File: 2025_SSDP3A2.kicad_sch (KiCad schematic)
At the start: 58 parts, among them J1 SolderPad, J2 SolderPad, J3 SolderPad, J4 SolderPad, Q1 CSD19534Q5A, Q2 BSC0805LS, U1 LM5146RGYR

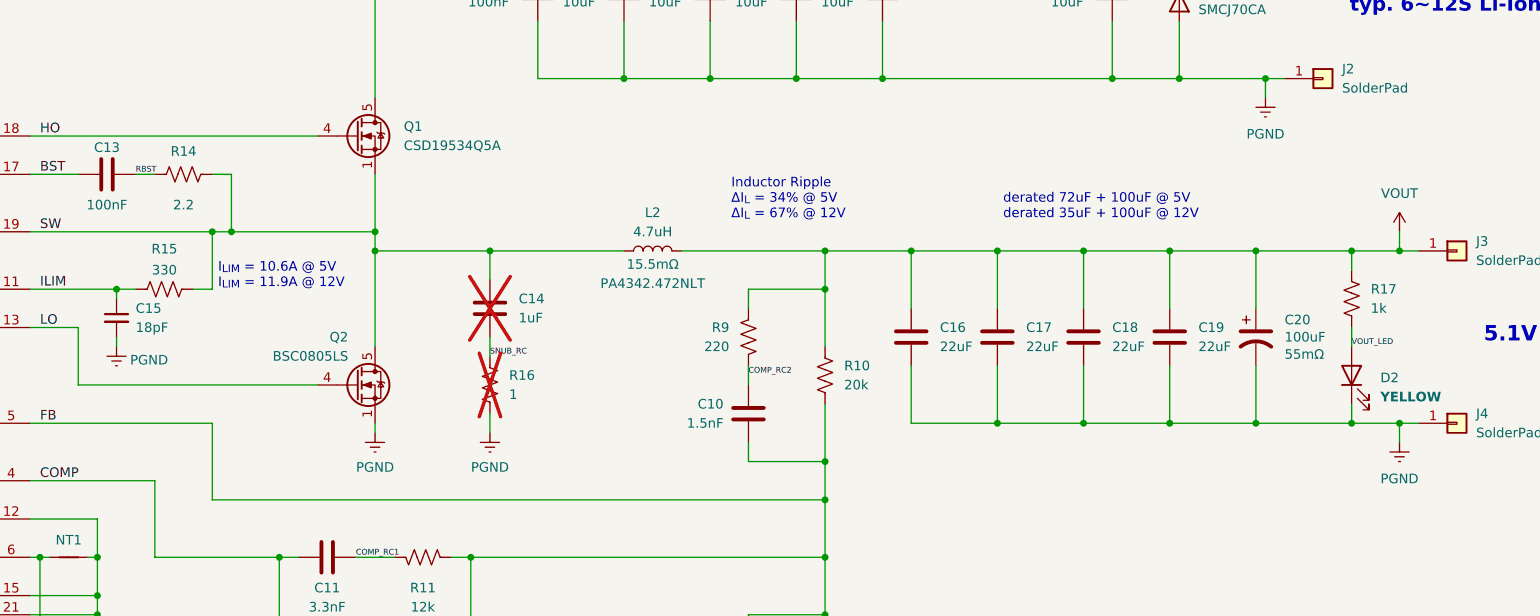
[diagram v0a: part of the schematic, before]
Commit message: Using PQFN FETs instead of SuperSO-8
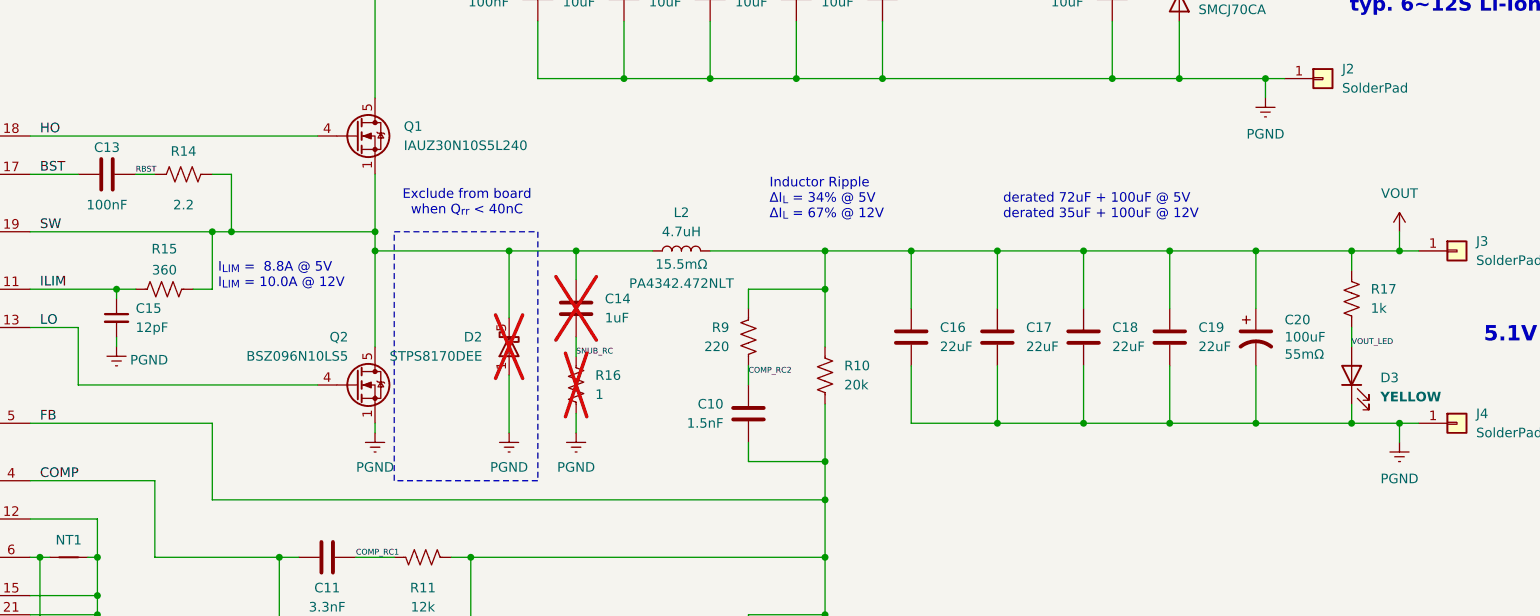
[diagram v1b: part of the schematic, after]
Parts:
- added D2: STPS8170DEE, TSDSON-8:PG-TSDSON-8-26, symbol Device:D_Schottky_AAK
- C15: value 18pF -> 12pF; LCSC PN C913624 -> C576801; MANUFACTURER Murata Electronics -> YAGEO
- Q1: value CSD19534Q5A -> IAUZ30N10S5L240; footprint Package_TO_SOT_SMD:TDSON-8-1 -> TSDSON-8:PG-TSDSON-8-26_TV; ESR 13.8mΩ -> 26.0mΩ; LCSC PN C114200 -> C535732; MANUFACTURER Texas Instruments -> Infineon Technologies
- Q2: value BSC0805LS -> BSZ096N10LS5; footprint Package_TO_SOT_SMD:TDSON-8-1 -> TSDSON-8:PG-TSDSON-8-26; ESR 7.1mΩ -> 9.6mΩ; LCSC PN C534374 -> C534695
- R15: value 330 -> 360; LCSC PN C23138 -> C25194; Part Type Basic -> Preferred Extended
- renumbered D2 to D3
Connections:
- net PGND: now also D2.1 (A), D2.2 (A), D2.3 (A)
- net SW: now also Q2.6 (D), Q2.7 (D), Q2.8 (D), D2.5 (K), D2.6, D2.7, D2.8
- net VIN: now also Q1.6 (D), Q1.7 (D), Q1.8 (D)
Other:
- note added: "Exclude from board when Q_{rr} < 40nC"
- note added: "I_{LIM} = 8.8A @ 5V I_{LIM} = 10.0A @ 12V"
- note removed: "I_{LIM} = 10.6A @ 5V I_{LIM} = 11.9A @ 12V"
- moved on the sheet: L2

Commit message: Finished routing
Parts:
- R7: value 27k -> 24k; LCSC PN C22967 -> C23352
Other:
- note added: "f_{SW} = 420kHz"
- note removed: "f_{SW} = 370kHz"
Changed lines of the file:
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@@
 		)
 	)
-	(text "f_{SW} = 370kHz"
+	(text "f_{SW} = 420kHz"
 		(exclude_from_sim no)
 		(at 69.85 135.636 0)
@@
 			)
 		)
-		(property "Value" "27k"
+		(property "Value" "24k"
 			(at 72.39 175.26 0)
 			(effects
@@
 			)
 		)
-		(property "Description" "0603WAF2702T5E"
+		(property "Description" "0603WAF2402T5E"
 			(at 69.85 173.99 0)
 			(effects
@@
 			)
 		)
-		(property "LCSC PN" "C22967"
+		(property "LCSC PN" "C23352"
 			(at 69.85 173.99 0)
 			(effects

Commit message: Tweaked routing, changed some fab parameters
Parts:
- Q1, Q2, U1: FT Rotation Offset -90 -> 0
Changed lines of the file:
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@@
 			)
 		)
-		(property "FT Rotation Offset" "-90"
+		(property "FT Rotation Offset" "0"
 			(at 114.3 116.84 0)
 			(effects
@@
 			)
 		)
-		(property "FT Rotation Offset" "-90"
+		(property "FT Rotation Offset" "0"
 			(at 203.2 116.84 0)
 			(effects
@@
 			)
 		)
-		(property "FT Rotation Offset" "-90"
+		(property "FT Rotation Offset" "0"
 			(at 203.2 149.86 0)
 			(effects

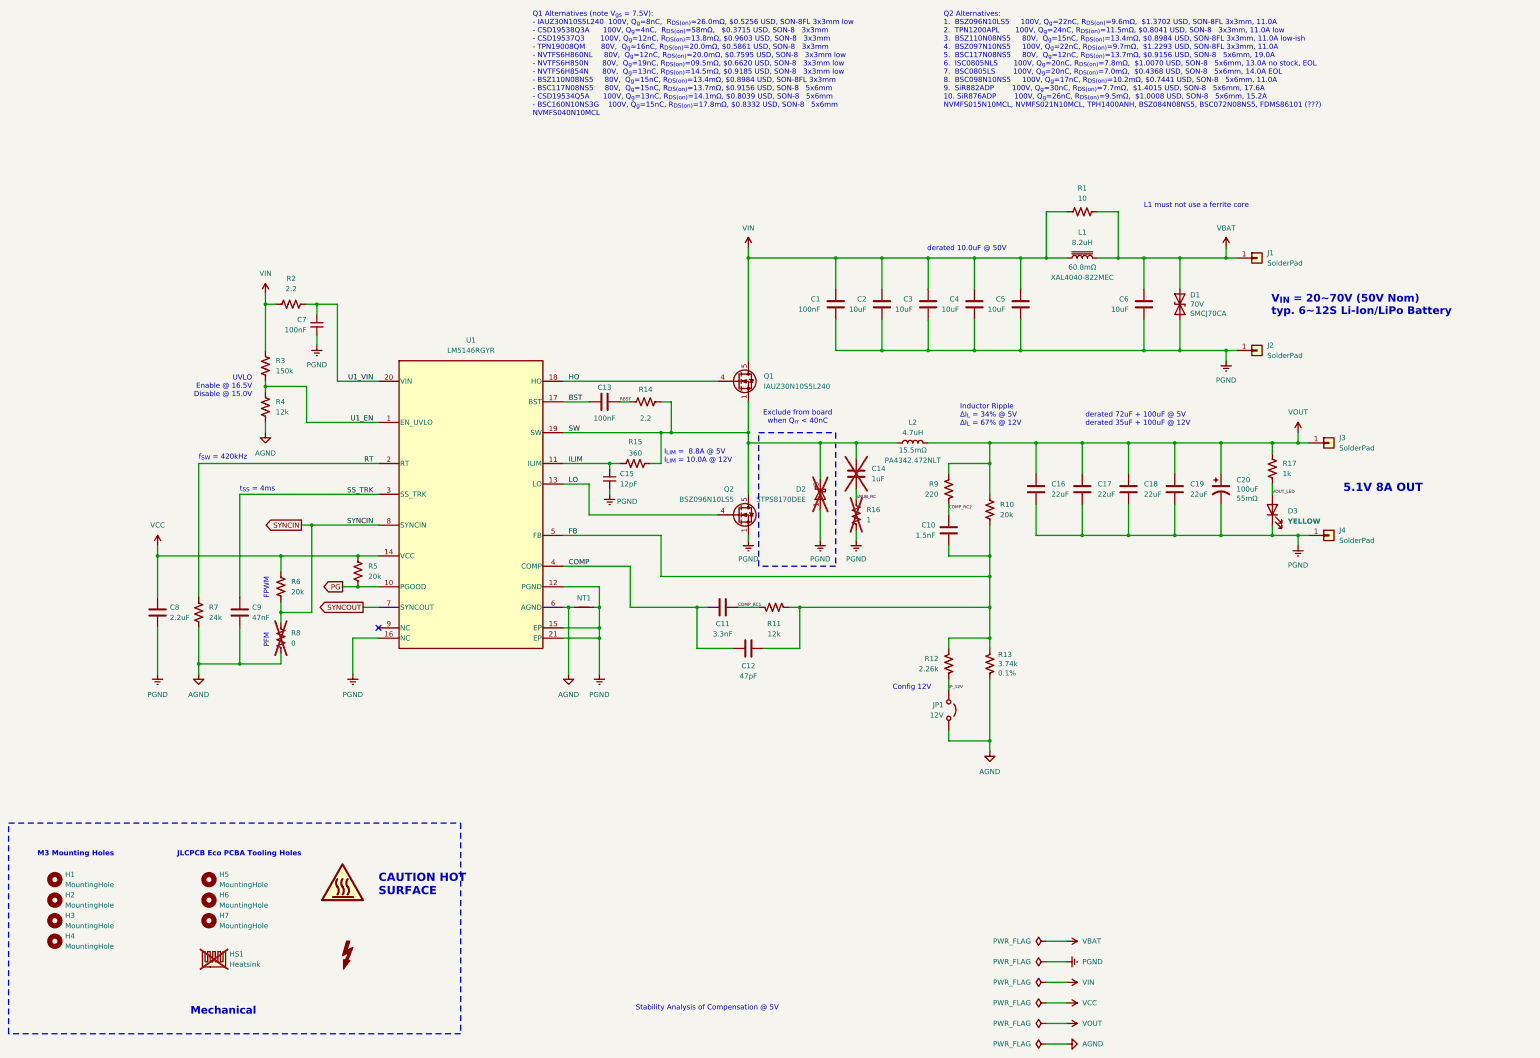
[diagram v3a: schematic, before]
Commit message: Tweaked feedback routing and removed EMI filter
The EMI filter places an inductor in between the battery and the buck
converter, creating the risk of resonance either at the buck converter
input or on the battery line. While the former issue has been *somewhat*
addressed with the parallel damping resistor, the latter issue cannot be
reasonably fixed without good knowledge of the other various loads that
may be attached to the battery line. For this reason, the EMI filter is
removed.
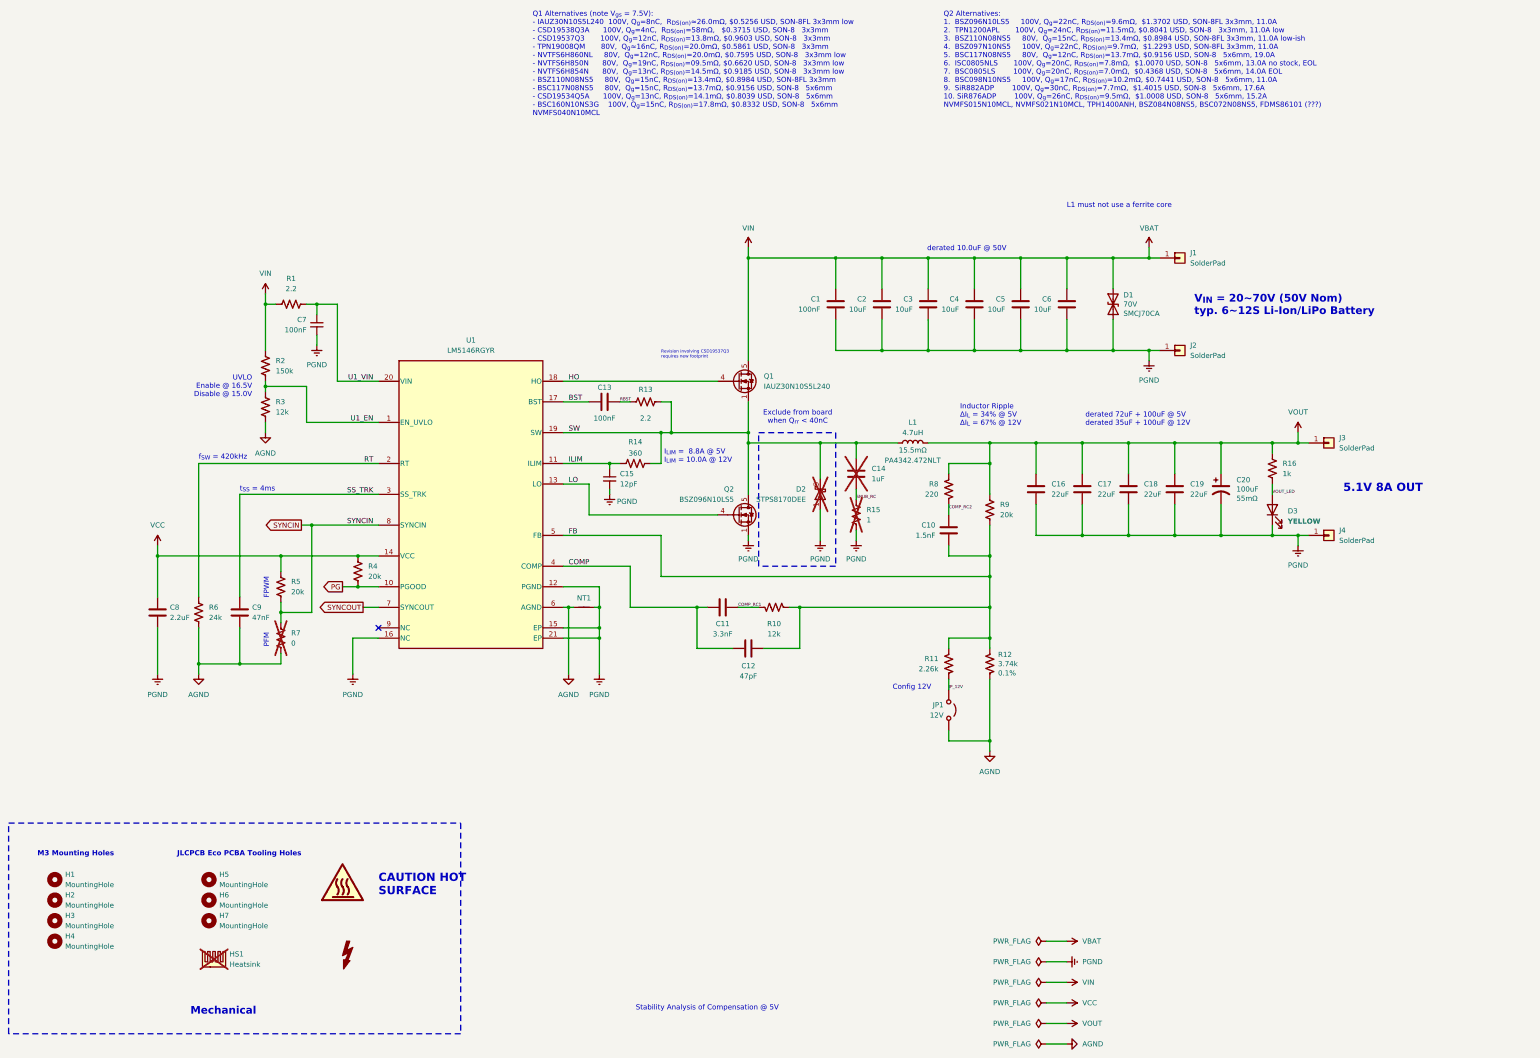
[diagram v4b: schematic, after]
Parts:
- removed L1: 8.2uH, Inductor_SMD:L_Coilcraft_XAL4040-XXX, symbol Device:L_Iron
- removed R1: 10, Resistor_SMD:R_0805_2012Metric_Pad1.20x1.40mm_HandSolder, symbol Device:R_US
- Q1: LCSC ALT1 (none) -> C478469; PART ALT1 (none) -> CSD19537Q3
- Q2: LCSC ALT1 (none) -> C534697; PART ALT1 (none) -> BSZ097N10NS5
- renumbered L2 to L1, R2 to R1, R11 to R10, R12 to R11, R13 to R12, R14 to R13, R15 to R14, R16 to R15, R17 to R16, R3 to R2, R4 to R3, R5 to R4, R6 to R5, R7 to R6, R8 to R7, R9 to R8, R10 to R9
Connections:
- net VIN is gone; now on net VBAT: C1.1, C2.1, C3.1, C4.1, C5.1, Q1.5 (D), Q1.6 (D), Q1.7 (D), Q1.8 (D), R1.1, R2.1
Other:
- note added: "Revision involving CSD19537Q3 requires new footprint"
- moved on the sheet: C6, D1, J1, J2

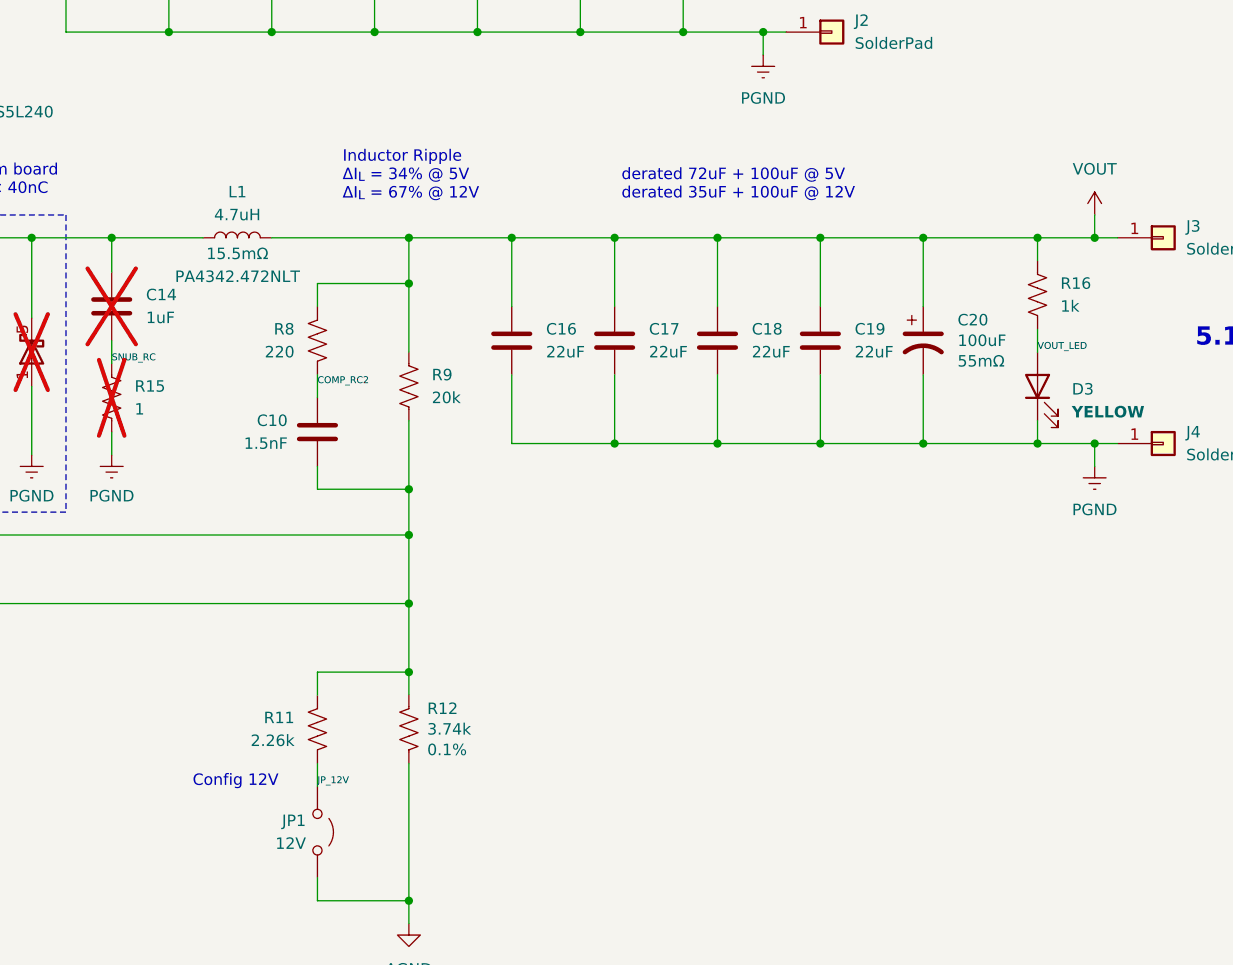
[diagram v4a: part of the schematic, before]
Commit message: Tweaked routing, added breakout pads, via clean up
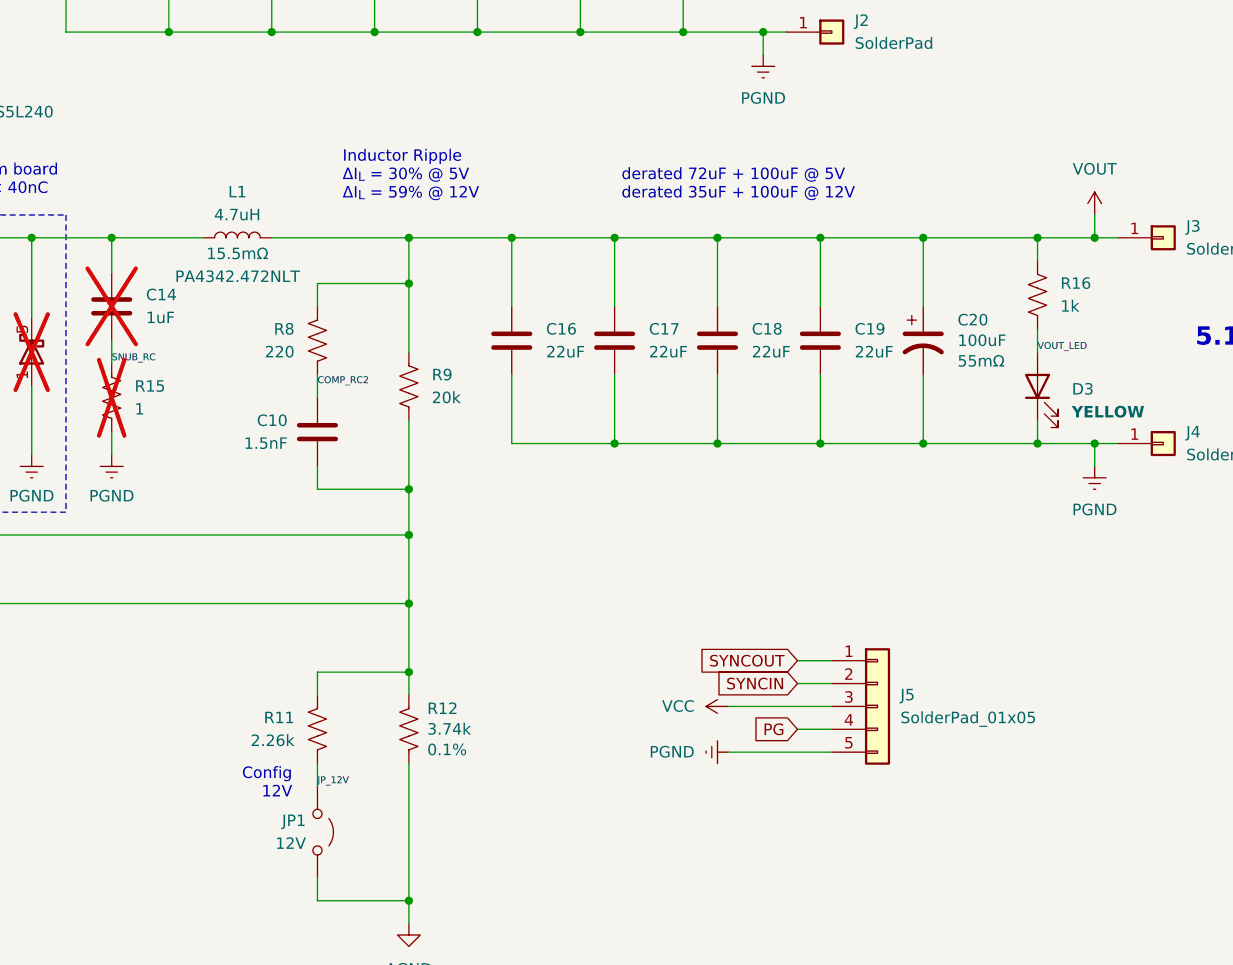
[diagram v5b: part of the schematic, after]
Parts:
- added J5: SolderPad_01x05, Connector_Custom:SolderWirePad_1x05_SMD_1.5x2mm, symbol Connector_Generic:Conn_01x05
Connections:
- net PG: now also J5.4 (Pin_4)
- net PGND: now also J5.5 (Pin_5)
- net SYNCIN: now also J5.2 (Pin_2)
- net SYNCOUT: now also J5.1 (Pin_1)
- net VCC: now also J5.3 (Pin_3)
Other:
- note added: "Inductor Ripple ΔI_{L} = 30% @ 5V ΔI_{L} = 59% @ 12V"
- note removed: "Inductor Ripple ΔI_{L} = 34% @ 5V ΔI_{L} = 67% @ 12V"
